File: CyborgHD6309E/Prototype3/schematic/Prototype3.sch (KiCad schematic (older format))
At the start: 29 parts, among them J1 Conn_I2C_Master, J2 Conn_Micro_SD, J3 Conn_USB_Serial, J4 Conn_AVR_ISP, J5 Conn_AVR_ISP, SW1 USR_SW, U1 ATmega1284P-PU, U2 HM628128DLP-5, U3 HD63C09E, U4 ATmega328P-PU, Y1 20MHz, Y2 20MHz

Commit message: [CyborgHD6309E] Update Prototype3 to libcli 1.0.4
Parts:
- J2: symbol 0-LocalLibrary:Conn_Micro_SD -> Prototype3-rescue:Conn_Micro_SD-0-LocalLibrary
- J3: symbol 0-LocalLibrary:Conn_USB_Serial -> Prototype3-rescue:Conn_USB_Serial-0-LocalLibrary
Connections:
- net A0: now also U2.12 (A0); no longer U2.26 (A9)
- net A1: now also U2.11 (A1); no longer U2.25 (A11)
- net A10: now also U2.23 (A10); no longer U2.10 (A2)
- net A11: now also U2.25 (A11); no longer U2.11 (A1)
- net A12: now also U2.4 (A12); no longer U2.12 (A0)
- net A13: now also U2.28 (A13); no longer U2.31 (A15)
- net A14: now also U2.3 (A14); no longer U2.28 (A13)
- net A15: now also U2.31 (A15); no longer U2.27 (A8)
- net A2: now also U2.10 (A2); no longer U2.23 (A10)
- net A3: now also U2.9 (A3); no longer U2.3 (A14)
- net A4: now also U2.8 (A4); no longer U2.4 (A12)
- net A5: now also U2.7 (A5); no longer U2.5 (A7)
- net A7: now also U2.5 (A7); no longer U2.7 (A5)
- net A8: now also U2.27 (A8); no longer U2.8 (A4)
- net A9: now also U2.26 (A9); no longer U2.9 (A3)
- net D0: now also U2.13 (Q0); no longer U2.21 (Q7)
- net D1: now also U2.14 (Q1); no longer U2.20 (Q6)
- net D2: now also U2.15 (Q2); no longer U2.19 (Q5)
- net D3: now also U2.17 (Q3); no longer U2.18 (Q4)
- net D4: now also U2.18 (Q4); no longer U2.17 (Q3)
- net D5: now also U2.19 (Q5); no longer U2.13 (Q0)
- net D6: now also U2.20 (Q6); no longer U2.14 (Q1)
- net D7: now also U2.21 (Q7); no longer U2.15 (Q2)
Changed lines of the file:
@@
 EESchema Schematic File Version 4
-EELAYER 30 0
+LIBS:Prototype3-cache
+EELAYER 26 0
 EELAYER END
 $Descr A4 11693 8268
@@
 	4050 1950 4150 2050
 Text Label 4250 2850 2    50   ~ 0
+A8
+Text Label 4250 3450 2    50   ~ 0
+A14
+Text Label 4250 3350 2    50   ~ 0
+A13
+Text Label 4250 3250 2    50   ~ 0
+A12
+Text Label 4250 3150 2    50   ~ 0
+A11
+Text Label 4250 3050 2    50   ~ 0
+A10
+Text Label 4250 2950 2    50   ~ 0
+A9
+Text Label 4250 3550 2    50   ~ 0
 A15
-Text Label 4250 3450 2    50   ~ 0
-A3
-Text Label 4250 3350 2    50   ~ 0
-A14
-Text Label 4250 3250 2    50   ~ 0
-A4
-Text Label 4250 3150 2    50   ~ 0
-A1
-Text Label 4250 3050 2    50   ~ 0
-A2
-Text Label 4250 2950 2    50   ~ 0
-A0
-Text Label 4250 3550 2    50   ~ 0
-A13
 Text Label 4250 2750 2    50   ~ 0
-A5
+A7
 Text Label 4250 2650 2    50   ~ 0
 A6
 Text Label 4250 2550 2    50   ~ 0
-A7
+A5
 Text Label 4250 2450 2    50   ~ 0
-A8
+A4
 Text Label 4250 2350 2    50   ~ 0
-A9
+A3
 Text Label 4250 2250 2    50   ~ 0
-A10
+A2
 Text Label 4250 2150 2    50   ~ 0
-A11
+A1
 Text Label 4250 2050 2    50   ~ 0
-A12
+A0
 $Comp
 L power:GND #PWR0106
@@
 	5350 2050 5450 1950
 Text Label 5250 2750 0    50   ~ 0
+D7
+Text Label 5250 2650 0    50   ~ 0
+D6
+Text Label 5250 2550 0    50   ~ 0
+D5
+Text Label 5250 2450 0    50   ~ 0
+D4
+Text Label 5250 2350 0    50   ~ 0
+D3
+Text Label 5250 2250 0    50   ~ 0
+D2
+Text Label 5250 2150 0    50   ~ 0
+D1
+Text Label 5250 2050 0    50   ~ 0
 D0
-Text Label 5250 2650 0    50   ~ 0
-D1
-Text Label 5250 2550 0    50   ~ 0
-D2
-Text Label 5250 2450 0    50   ~ 0
-D3
-Text Label 5250 2350 0    50   ~ 0
-D4
-Text Label 5250 2250 0    50   ~ 0
-D7
-Text Label 5250 2150 0    50   ~ 0
-D6
-Text Label 5250 2050 0    50   ~ 0
-D5
 Entry Wire Line
 	8350 2650 8450 2750
@@
 Connection ~ 1250 5350
 $Comp
-L 0-LocalLibrary:Conn_Micro_SD J2
+L Prototype3-rescue:Conn_Micro_SD-0-LocalLibrary J2
 U 1 1 5D0A3A84
 P 6050 5750
@@
 $EndComp
 $Comp
-L 0-LocalLibrary:Conn_USB_Serial J3
+L Prototype3-rescue:Conn_USB_Serial-0-LocalLibrary J3
 U 1 1 5D0B116C
 P 9300 5800

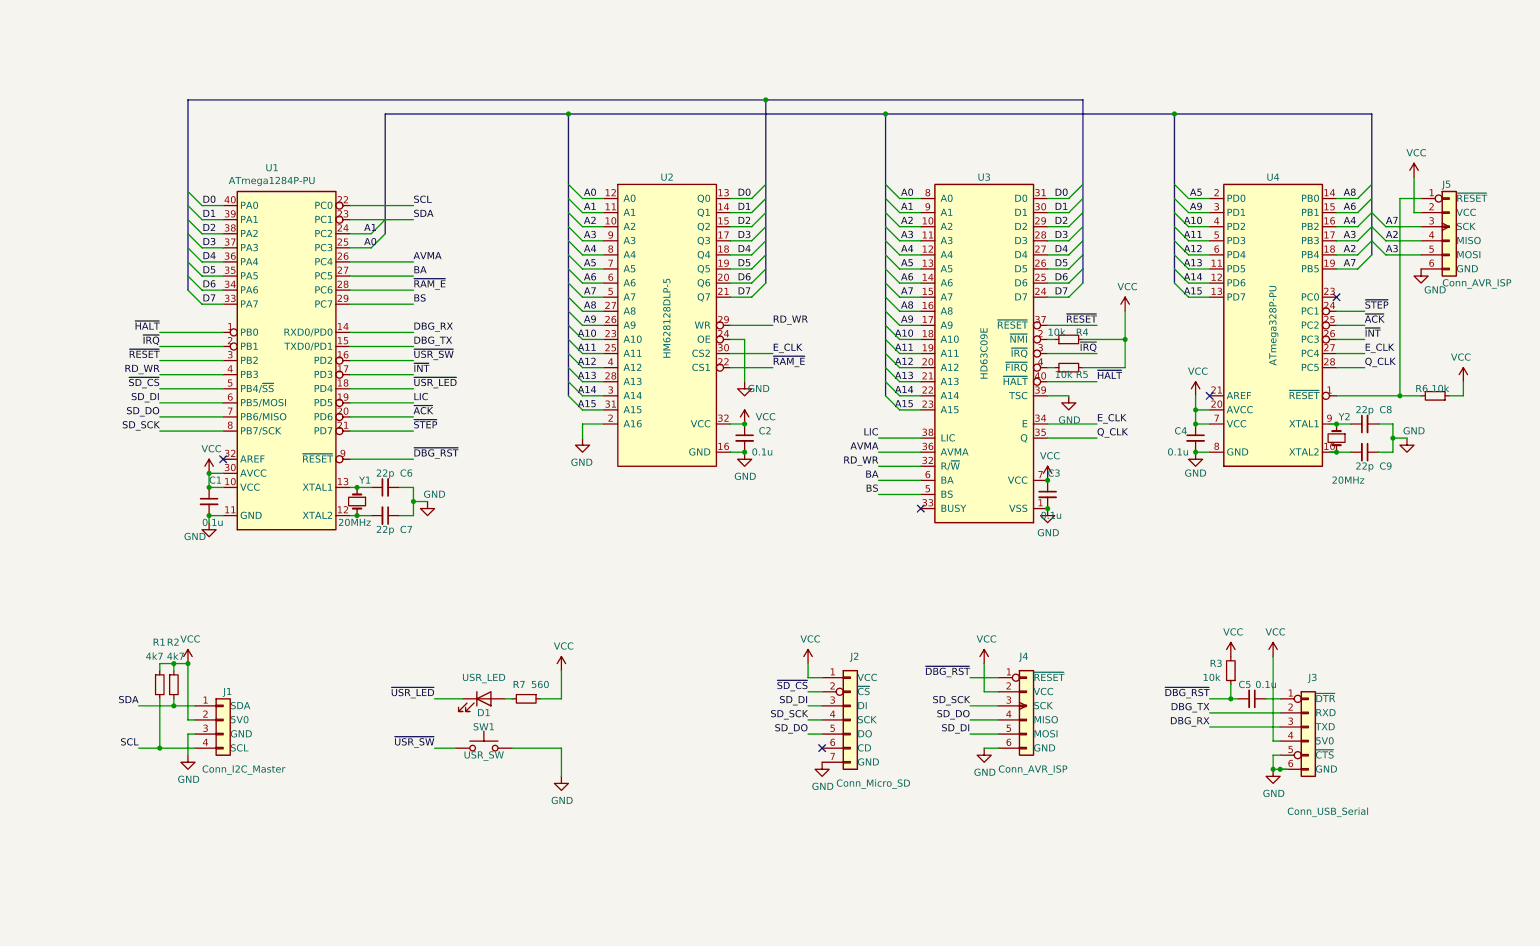
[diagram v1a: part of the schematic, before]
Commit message: [CyborgHD6309E] Update Prototype3 pins
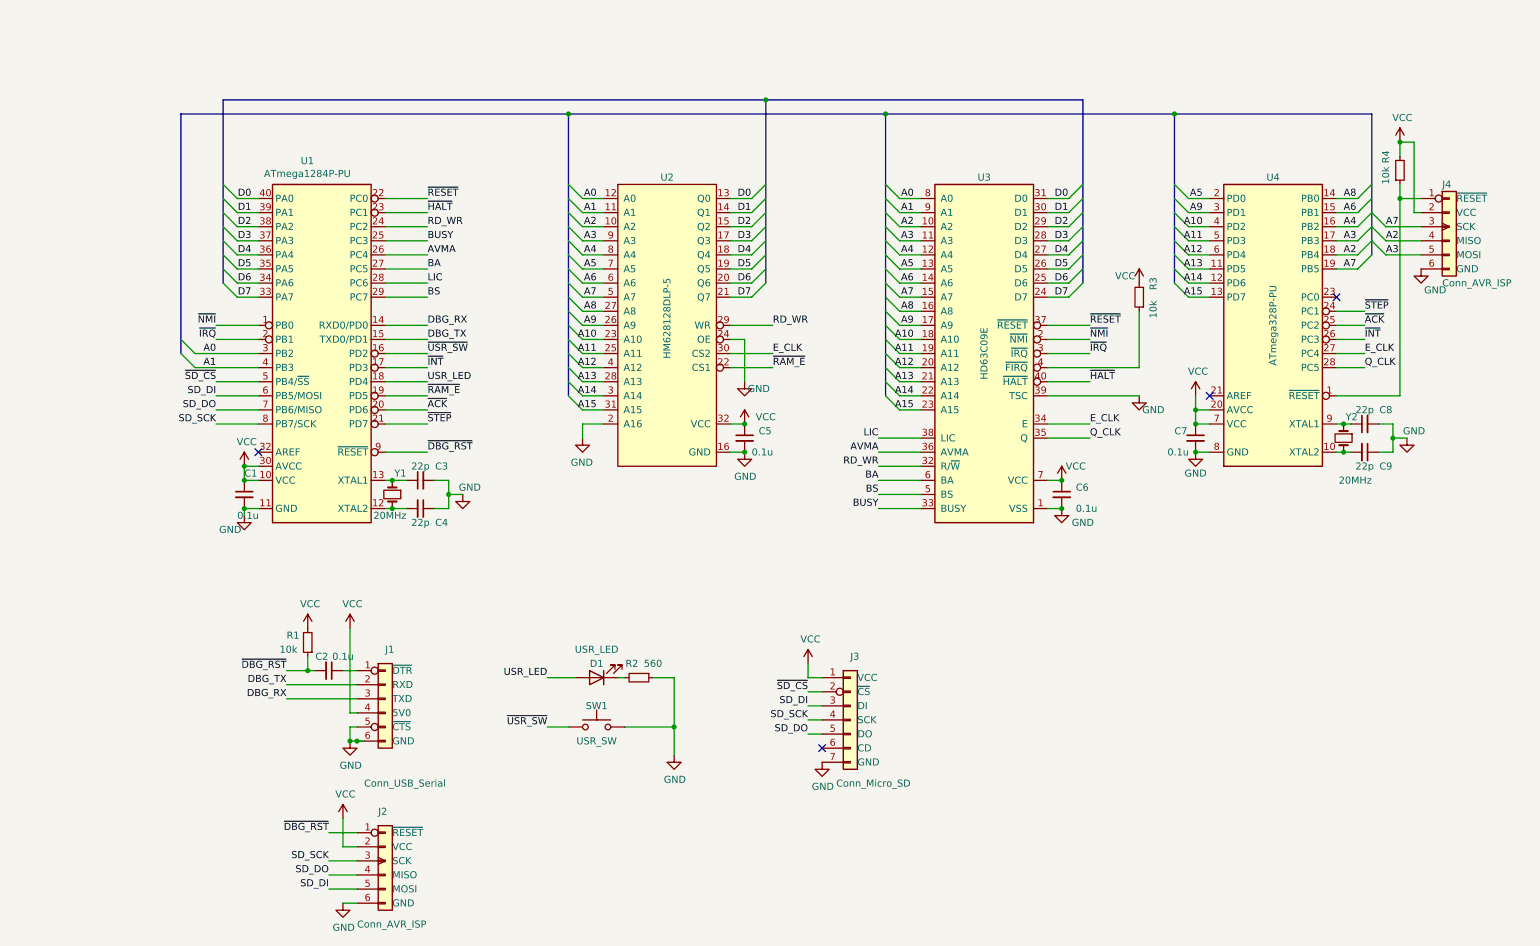
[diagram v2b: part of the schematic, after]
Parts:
- removed J1: Conn_I2C_Master, Connector_PinSocket_2.54mm:PinSocket_1x04_P2.54mm_Vertical, symbol 0-LocalLibrary:Conn_I2C_Master
- removed R1, R2: 4k7, Resistor_SMD:R_0603_1608Metric, symbol Device:R_Small
- removed R4: 10k, Resistor_SMD:R_0603_1608Metric, symbol Device:R_Small
- renumbered C5 to C2, C6 to C3, C7 to C4, C2 to C5, C3 to C6, C4 to C7, J3 to J1, J4 to J2, J2 to J3, J5 to J4, R3 to R1, R7 to R2, R5 to R3, R6 to R4
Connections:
- net A0: now also U1.3 (PB2); no longer U1.25 (PC3)
- net A1: now also U1.4 (PB3); no longer U1.24 (PC2)
- net GND: now also R2.1
- net LIC: now also U1.28 (PC6); no longer U1.19 (PD5)
- net RD_WR: now also U1.24 (PC2); no longer U1.4 (PB3)
- net VCC: now also R4.2; no longer R2.1, R4.1
- net ~NMI~: now reaches U3.2 (~NMI)
- net ~NMI~: now also U1.1 (PB0)
- net BUSY: now reaches U3.33 (BUSY)
- net BUSY: now also U1.25 (PC3)
- net at J4.1 (~RESET~), U4.1 (~RESET~): now also R4.1; no longer R4.2
- net at R2.2: now also D1.1 (K); no longer D1.2 (A)
- net SCL renamed ~RESET~
- net ~RESET~: now also U3.37 (~RESET)
- net SDA renamed ~HALT~
- net ~HALT~: now also U3.40 (~HALT)
- net ~ACK renamed ~ACK~
- removed net ~HALT: U1.1 (PB0), U3.40 (~HALT)
- net ~INT renamed ~INT~
- net ~RAM_E renamed ~RAM_E~
- net ~RAM_E~: now also U1.19 (PD5); no longer U1.28 (PC6)
- removed net ~RESET: U1.3 (PB2), U3.37 (~RESET)
- net ~SD_CS renamed ~SD_CS~
- net ~STEP renamed ~STEP~
- net ~USR_LED~ renamed USR_LED
- net USR_LED: now also D1.2 (A); no longer D1.1 (K)
- no-connect marks 5 -> 4
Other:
- moved on the sheet: C1, C2, C3, C4, C6, D1, J1, J2, R1, R2, R3, R4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
